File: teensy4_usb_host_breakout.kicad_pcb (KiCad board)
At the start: 2 copper layers, 24.1 x 15.2 mm, 11 parts, among them J1 Conn_01x06, J2 USB_A, U1 TPD3S014

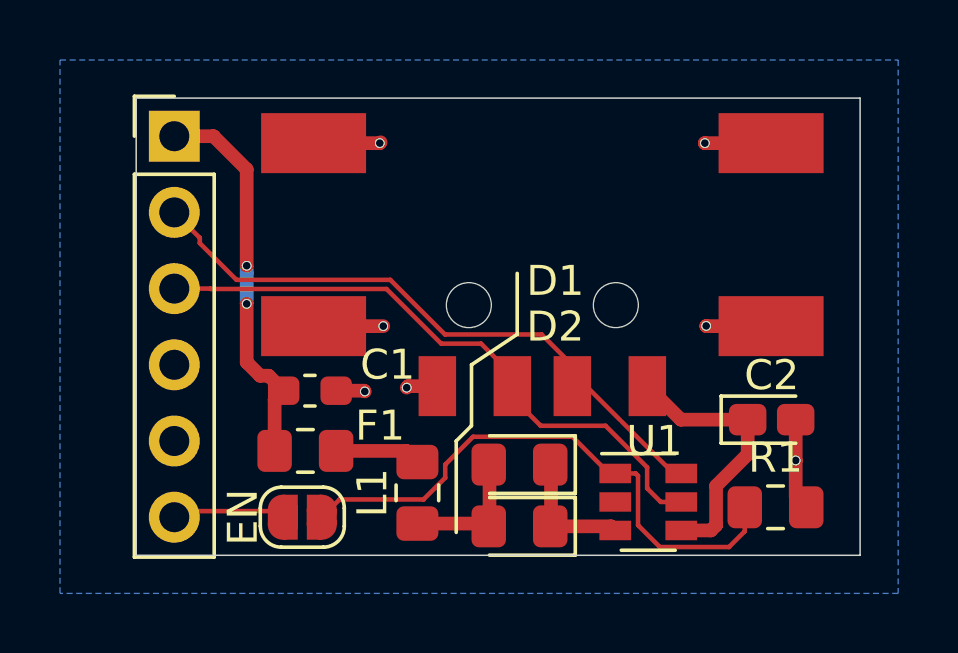
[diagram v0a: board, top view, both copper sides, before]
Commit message: Update footprintso
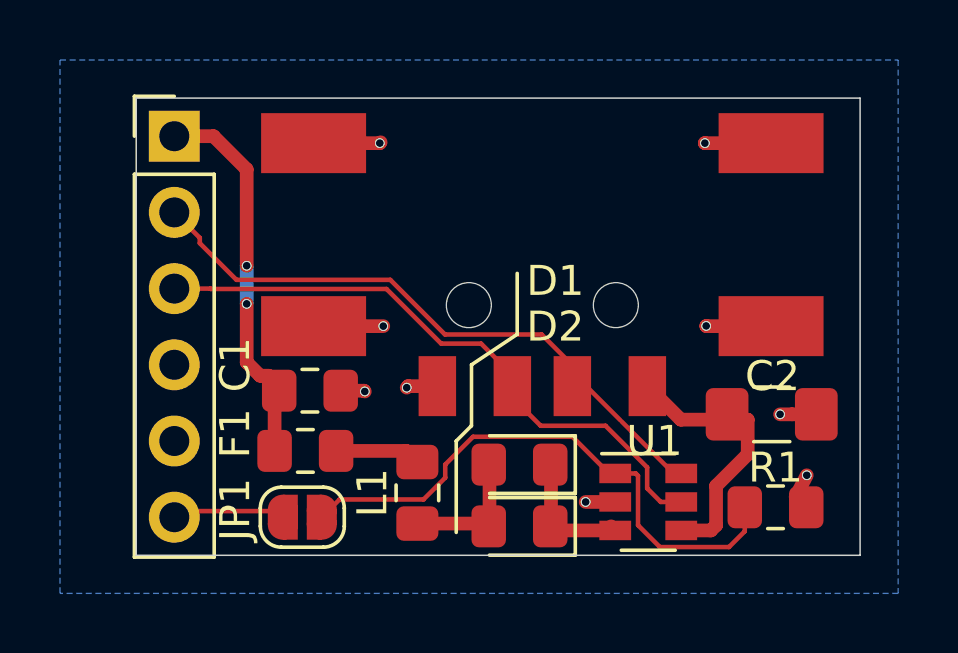
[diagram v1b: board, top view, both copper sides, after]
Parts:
- C1: footprint Capacitor_SMD:C_0603_1608Metric_Pad1.05x0.95mm_HandSolder -> Capacitor_SMD:C_0805_2012Metric_Pad1.15x1.40mm_HandSolder
- C2: footprint Capacitor_Tantalum_SMD:CP_EIA-1608-08_AVX-J_Pad1.25x1.05mm_HandSolder -> Capacitor_SMD:C_1206_3216Metric_Pad1.42x1.75mm_HandSolder
- JP1: renamed from EN; value SolderJumper_2_Open -> EN
- moved C2 0.18 mm to (178.7, 113.4)
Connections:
- U1 pad 2: (no net) -> GND
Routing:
- net GND: track 14.0 -> 14.5 mm, vias 7 -> 9
